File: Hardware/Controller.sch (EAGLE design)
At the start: 12 parts

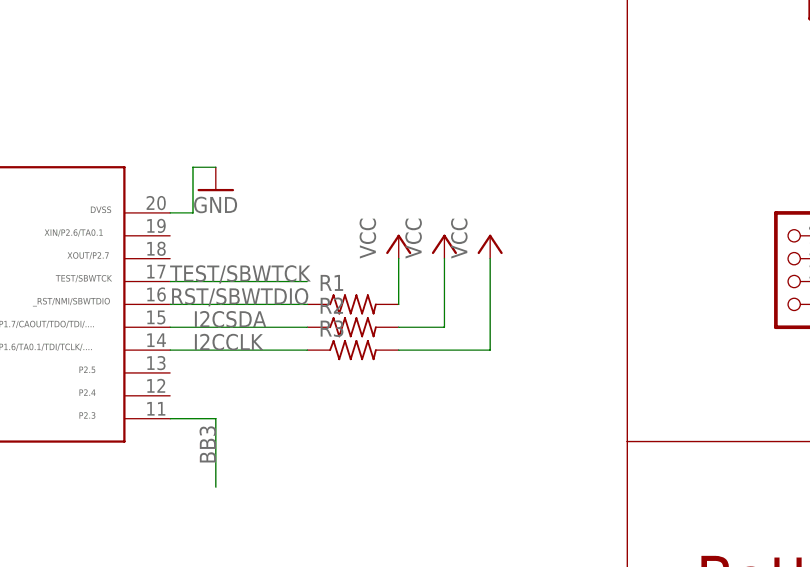
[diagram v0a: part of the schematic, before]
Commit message: removed extra i2c resistors
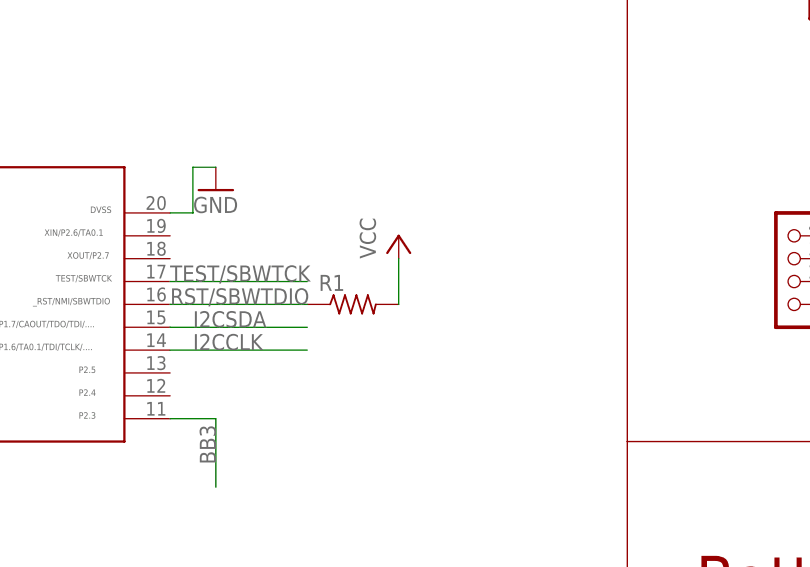
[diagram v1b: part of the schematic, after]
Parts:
- removed R2, R3: (no value), rcl:R-US_R1206
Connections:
- net I2CCLK: no longer R3.1
- net I2CSDA: no longer R2.1
- net VCC: no longer R2.2, R3.2
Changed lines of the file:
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@@
 <part name="P+2" library="supply1" library_urn="urn:adsk.eagle:library:371" deviceset="VCC" device=""/>
 <part name="GND1" library="supply1" library_urn="urn:adsk.eagle:library:371" deviceset="GND" device=""/>
-<part name="R2" library="rcl" library_urn="urn:adsk.eagle:library:334" deviceset="R-US_" device="R1206" package3d_urn="urn:adsk.eagle:package:23540/2"/>
-<part name="R3" library="rcl" library_urn="urn:adsk.eagle:library:334" deviceset="R-US_" device="R1206" package3d_urn="urn:adsk.eagle:package:23540/2"/>
-<part name="P+3" library="supply1" library_urn="urn:adsk.eagle:library:371" deviceset="VCC" device=""/>
-<part name="P+4" library="supply1" library_urn="urn:adsk.eagle:library:371" deviceset="VCC" device=""/>
 <part name="JP1" library="pinhead" library_urn="urn:adsk.eagle:library:325" deviceset="PINHD-1X1" device="" package3d_urn="urn:adsk.eagle:package:22485/2"/>
 <part name="JP2" library="pinhead" library_urn="urn:adsk.eagle:library:325" deviceset="PINHD-1X1" device="" package3d_urn="urn:adsk.eagle:package:22485/2"/>
@@
 <instance part="GND1" gate="1" x="78.74" y="58.42" smashed="yes">
 <attribute name="VALUE" x="76.2" y="55.88" size="1.778" layer="96"/>
-</instance>
-<instance part="R2" gate="G$1" x="93.98" y="43.18" smashed="yes">
-<attribute name="NAME" x="90.17" y="44.6786" size="1.778" layer="95"/>
-<attribute name="VALUE" x="90.17" y="39.878" size="1.778" layer="96"/>
-</instance>
-<instance part="R3" gate="G$1" x="93.98" y="40.64" smashed="yes">
-<attribute name="NAME" x="90.17" y="42.1386" size="1.778" layer="95"/>
-<attribute name="VALUE" x="90.17" y="37.338" size="1.778" layer="96"/>
-</instance>
-<instance part="P+3" gate="VCC" x="104.14" y="53.34" smashed="yes">
-<attribute name="VALUE" x="101.6" y="50.8" size="1.778" layer="96" rot="R90"/>
-</instance>
-<instance part="P+4" gate="VCC" x="109.22" y="53.34" smashed="yes">
-<attribute name="VALUE" x="106.68" y="50.8" size="1.778" layer="96" rot="R90"/>
 </instance>
 <instance part="JP1" gate="G$1" x="147.32" y="78.74" smashed="yes" rot="R270">
@@
 <wire x1="73.66" y1="43.18" x2="88.9" y2="43.18" width="0.1524" layer="91"/>
 <label x="76.2" y="43.18" size="1.778" layer="95"/>
-<pinref part="R2" gate="G$1" pin="1"/>
 </segment>
 <segment>
@@
 <wire x1="73.66" y1="40.64" x2="88.9" y2="40.64" width="0.1524" layer="91"/>
 <label x="76.2" y="40.64" size="1.778" layer="95"/>
-<pinref part="R3" gate="G$1" pin="1"/>
 </segment>
 <segment>
@@
 </segment>
 <segment>
-<pinref part="R2" gate="G$1" pin="2"/>
-<wire x1="99.06" y1="43.18" x2="104.14" y2="43.18" width="0.1524" layer="91"/>
-<wire x1="104.14" y1="43.18" x2="104.14" y2="50.8" width="0.1524" layer="91"/>
-<pinref part="P+3" gate="VCC" pin="VCC"/>
-</segment>
-<segment>
-<pinref part="R3" gate="G$1" pin="2"/>
-<wire x1="99.06" y1="40.64" x2="109.22" y2="40.64" width="0.1524" layer="91"/>
-<wire x1="109.22" y1="40.64" x2="109.22" y2="50.8" width="0.1524" layer="91"/>
-<pinref part="P+4" gate="VCC" pin="VCC"/>
-</segment>
-<segment>
